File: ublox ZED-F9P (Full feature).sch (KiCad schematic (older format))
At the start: 99 parts, among them J1 USB_C_2-LAYER_PADS, J2 CONN_06NO_SILK_FEMALE_PTH, J3 Molex_PicoBlade, J4 PinHeader, J5 USB_C_2-LAYER_PADS, J6 CONN_06NO_SILK_FEMALE_PTH, J7 JST_GH, U1 LD1117S33TR, U3 ZED-F9P, U4 ZED-F9H

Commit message: part no updated
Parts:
- removed J3: Molex_PicoBlade, Connector_Molex:Molex_PicoBlade_53261-0671_1x06-1MP_P1.25mm_Horizontal, symbol Connector:Conn_01x06_Male
- removed JP1, JP2, JP3, JP4: Jumper_NO_Small, Jumper:SolderJumper-2_P1.3mm_Open_RoundedPad1.0x1.5mm, symbol Device:Jumper_NO_Small
- removed LED1: RED, Qwiic GPS-RTK-SMA - ublox ZED-F9P:LED-0603, symbol ublox-ZED-F9P-(Full-feature)-rescue:LED-RED0603-Qwiic_GPS-RTK-SMA_-_ublox_ZED-F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
- removed PPS1, PWR2: JUMPER-SMT_2_NC_TRACE_SILK, Qwiic GPS-RTK-SMA - ublox ZED-F9P:SMT-JUMPER_2_NC_TRACE_SILK, symbol ublox-ZED-F9P-(Full-feature)-rescue:JUMPER-SMT_2_NC_TRACE_SILK-Qwiic_GPS-RTK-SM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
- removed R34: 1k, Qwiic GPS-RTK-SMA - ublox ZED-F9P:0603, symbol ublox-ZED-F9P-(Full-feature)-rescue:1KOHM-0603-1_10W-1%-Qwiic_GPS-RTK-SMA_-_ubl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
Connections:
- net at R21.1: now also E2.SIG (SIGNAL), U3.53 (TIMEPULSE)
- net RX(#4) renamed RX_P
- net RX(#5) renamed RX_H
- net TX(#4) renamed TX_P
- net TX(#5) renamed TX_H
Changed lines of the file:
@@
 Wire Wire Line
 	10775 2925 10475 2925
-Wire Wire Line
-	13425 6925 13425 6825
-Text Label 13425 6925 0    10   ~ 0
-3.3V
-Wire Wire Line
-	13425 8325 13425 8225
-Text Label 13425 8325 0    10   ~ 0
-GND
-Wire Wire Line
-	13425 7925 13425 7825
-Wire Wire Line
-	13425 7325 13425 7425
-$Comp
-L ublox-ZED-F9P-(Full-feature)-rescue:1KOHM-0603-1_10W-1%-Qwiic_GPS-RTK-SMA_-_ublox_ZED-F9P-eagle-import R34
-U 1 1 5F77C25B
-P 13425 7625
-F 0 "R34" H 13280 7540 70  0000 C BNN
-F 1 "1k" H 13605 7605 70  0000 C TNN
-F 2 "Qwiic GPS-RTK-SMA - ublox ZED-F9P:0603" H 13425 7625 50  0001 C CNN
-F 3 "" H 13425 7625 50  0001 C CNN
-F 4 "ERJ-3EKF1001V" H 13425 7625 50  0001 C CNN "partno"
-	1    13425 7625
-	0    -1   -1   0
-$EndComp
-$Comp
-L ublox-ZED-F9P-(Full-feature)-rescue:LED-RED0603-Qwiic_GPS-RTK-SMA_-_ublox_ZED-F9P-eagle-import LED1
-U 1 1 5F77C265
-P 13425 8025
-F 0 "LED1" V 13410 7645 70  0000 L BNN
-F 1 "RED" V 13445 7705 70  0000 L TNN
-F 2 "Qwiic GPS-RTK-SMA - ublox ZED-F9P:LED-0603" H 13425 8025 50  0001 C CNN
-F 3 "" H 13425 8025 50  0001 C CNN
-F 4 "HSMH-C191" H 13425 8025 50  0001 C CNN "partno"
-	1    13425 8025
-	1    0    0    -1
-$EndComp
-$Comp
-L ublox-ZED-F9P-(Full-feature)-rescue:GND-Qwiic_GPS-RTK-SMA_-_ublox_ZED-F9P-eagle-import #GND0110
-U 1 1 5F77C26F
-P 13425 8425
-F 0 "#GND0110" H 13425 8425 50  0001 C CNN
-F 1 "GND" H 13325 8325 59  0000 L BNN
-F 2 "" H 13425 8425 50  0001 C CNN
-F 3 "" H 13425 8425 50  0001 C CNN
-	1    13425 8425
-	1    0    0    -1
-$EndComp
-$Comp
-L ublox-ZED-F9P-(Full-feature)-rescue:3.3V-Qwiic_GPS-RTK-SMA_-_ublox_ZED-F9P-eagle-import #P+0101
-U 1 1 5F77C279
-P 13425 6825
-F 0 "#P+0101" H 13425 6825 50  0001 C CNN
-F 1 "3.3V" H 13425 6935 59  0000 C BNN
-F 2 "" H 13425 6825 50  0001 C CNN
-F 3 "" H 13425 6825 50  0001 C CNN
-	1    13425 6825
-	1    0    0    -1
-$EndComp
-$Comp
-L ublox-ZED-F9P-(Full-feature)-rescue:JUMPER-SMT_2_NC_TRACE_SILK-Qwiic_GPS-RTK-SMA_-_ublox_ZED-F9P-eagle-import PWR2
-U 1 1 5F77C283
-P 13425 7125
-F 0 "PWR2" H 13345 7195 70  0000 L BNN
-F 1 "JUMPER-SMT_2_NC_TRACE_SILK" H 13325 7025 70  0000 L TNN
-F 2 "Qwiic GPS-RTK-SMA - ublox ZED-F9P:SMT-JUMPER_2_NC_TRACE_SILK" H 13425 7125 50  0001 C CNN
-F 3 "" H 13425 7125 50  0001 C CNN
-F 4 "-" H 13425 7125 50  0001 C CNN "partno"
-	1    13425 7125
-	0    -1   -1   0
-$EndComp
 Text Notes 13825 5100 0    85   ~ 17
 Stat LEDs (F9H)
@@
 Wire Wire Line
 	12625 2725 12775 2725
-$Comp
-L Connector:Conn_01x06_Male J3
-U 1 1 5F708564
-P 16425 2900
-F 0 "J3" H 16531 3278 50  0000 C CNN
-F 1 "Molex_PicoBlade" H 16250 3200 50  0000 C CNN
-F 2 "Connector_Molex:Molex_PicoBlade_53261-0671_1x06-1MP_P1.25mm_Horizontal" H 16425 2900 50  0001 C CNN
-F 3 "https://www.digikey.com/product-detail/en/molex/0532610671/WM7624CT-ND/699111" H 16425 2900 50  0001 C CNN
-F 4 "0532610671" H 16425 2900 50  0001 C CNN "partno"
-F 5 "Connector Header Surface Mount, Right Angle 6 position 0.049\" (1.25mm)" H 16425 2900 50  0001 C CNN "Detailed Description"
-F 6 "Approved" H 16425 2900 50  0001 C CNN "Approval"
-	1    16425 2900
-	1    0    0    -1
-$EndComp
 $Comp
 L Connector:Conn_01x06_Male J4
@@
 	1    0    0    -1
 $EndComp
-Wire Wire Line
-	16625 2700 16875 2700
 Connection ~ 16875 2700
 Wire Wire Line
@@
 Wire Wire Line
 	16875 2700 16875 3525
-Text Label 17225 2700 0    50   ~ 0
-Vcc
-Wire Wire Line
-	16625 3200 17250 3200
 Wire Wire Line
 	17250 3200 17500 3200
-Connection ~ 17250 3200
 Wire Wire Line
 	17250 4025 17250 3200
@@
 Wire Wire Line
 	17175 3100 17175 3925
-Text Label 17225 2800 0    50   ~ 0
-RX(#4)
-Text Label 17225 2900 0    50   ~ 0
-TX(#4)
-Text Label 17225 3000 0    50   ~ 0
-RX(#5)
-Text Label 17225 3100 0    50   ~ 0
-TX(#5)
-Text Label 17225 3200 0    50   ~ 0
-GND
 Wire Notes Line
 	15850 1950 15850 4250
@@
 	16875 2525 16875 2700
 $Comp
-L Device:Jumper_NO_Small JP1
-U 1 1 5F7085B9
-P 16725 2800
-F 0 "JP1" H 16725 2850 50  0000 C CNN
-F 1 "Jumper_NO_Small" H 16725 2894 50  0001 C CNN
-F 2 "Jumper:SolderJumper-2_P1.3mm_Open_RoundedPad1.0x1.5mm" H 16725 2800 50  0001 C CNN
-F 3 "~" H 16725 2800 50  0001 C CNN
-F 4 "Approved" H 16725 2800 50  0001 C CNN "Approval"
-F 5 "-" H 16725 2800 50  0001 C CNN "partno"
-	1    16725 2800
-	1    0    0    -1
-$EndComp
-Wire Wire Line
-	16825 2800 16950 2800
-$Comp
-L Device:Jumper_NO_Small JP2
-U 1 1 5F7085C1
-P 16725 2900
-F 0 "JP2" H 16725 2950 50  0000 C CNN
-F 1 "Jumper_NO_Small" H 16725 2994 50  0001 C CNN
-F 2 "Jumper:SolderJumper-2_P1.3mm_Open_RoundedPad1.0x1.5mm" H 16725 2900 50  0001 C CNN
-F 3 "~" H 16725 2900 50  0001 C CNN
-F 4 "Approved" H 16725 2900 50  0001 C CNN "Approval"
-F 5 "-" H 16725 2900 50  0001 C CNN "partno"
-	1    16725 2900
-	1    0    0    -1
-$EndComp
-Wire Wire Line
-	16825 2900 17025 2900
-$Comp
-L Device:Jumper_NO_Small JP3
-U 1 1 5F7085C9
-P 16725 3000
-F 0 "JP3" H 16725 3050 50  0000 C CNN
-F 1 "Jumper_NO_Small" H 16725 3094 50  0001 C CNN
-F 2 "Jumper:SolderJumper-2_P1.3mm_Open_RoundedPad1.0x1.5mm" H 16725 3000 50  0001 C CNN
-F 3 "~" H 16725 3000 50  0001 C CNN
-F 4 "Approved" H 16725 3000 50  0001 C CNN "Approval"
-F 5 "-" H 16725 3000 50  0001 C CNN "partno"
-	1    16725 3000
-	1    0    0    -1
-$EndComp
-Wire Wire Line
-	16825 3000 17100 3000
-$Comp
-L Device:Jumper_NO_Small JP4
-U 1 1 5F7085D1
-P 16725 3100
-F 0 "JP4" H 16725 3150 50  0000 C CNN
-F 1 "Jumper_NO_Small" H 16725 3194 50  0001 C CNN
-F 2 "Jumper:SolderJumper-2_P1.3mm_Open_RoundedPad1.0x1.5mm" H 16725 3100 50  0001 C CNN
-F 3 "~" H 16725 3100 50  0001 C CNN
-F 4 "Approved" H 16725 3100 50  0001 C CNN "Approval"
-F 5 "-" H 16725 3100 50  0001 C CNN "partno"
-	1    16725 3100
-	1    0    0    -1
-$EndComp
-Wire Wire Line
-	16825 3100 17175 3100
-$Comp
 L Device:Jumper_NO_Small JP5
 U 1 1 5F7085D9
@@
 $EndComp
 Wire Wire Line
-	6100 3600 6000 3600
-Wire Wire Line
-	5500 3600 5600 3600
-$Comp
-L ublox-ZED-F9P-(Full-feature)-rescue:JUMPER-SMT_2_NC_TRACE_SILK-Qwiic_GPS-RTK-SMA_-_ublox_ZED-F9P-eagle-import PPS1
-U 1 1 E4382B22
-P 5800 3600
-F 0 "PPS1" H 5900 3740 70  0000 R TNN
-F 1 "JUMPER-SMT_2_NC_TRACE_SILK" H 5700 3500 70  0000 L TNN
-F 2 "Qwiic GPS-RTK-SMA - ublox ZED-F9P:SMT-JUMPER_2_NC_TRACE_SILK" H 5800 3600 50  0001 C CNN
-F 3 "" H 5800 3600 50  0001 C CNN
-F 4 "-" H 5800 3600 50  0001 C CNN "partno"
-	1    5800 3600
-	-1   0    0    1
-$EndComp
-Wire Wire Line
 	10000 6725 10375 6725
 Wire Wire Line
@@
 	1    0    0    1
 $EndComp
+Text Label 17225 2800 0    50   ~ 0
+RX_P
+Text Label 17225 2900 0    50   ~ 0
+TX_P
+Text Label 17225 3000 0    50   ~ 0
+RX_H
+Text Label 17225 3100 0    50   ~ 0
+TX_H
+Text Label 17225 2700 0    50   ~ 0
+Vcc
+Wire Wire Line
+	5500 3600 6100 3600
 $EndSCHEMATC

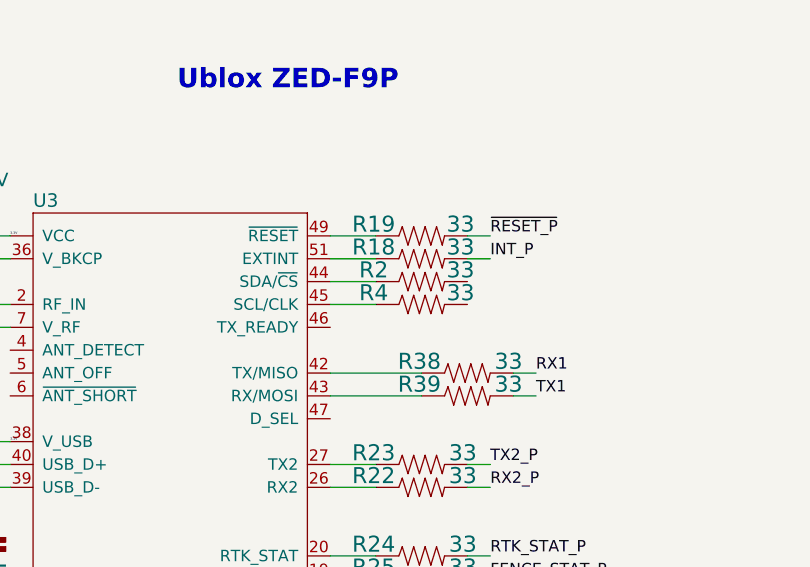
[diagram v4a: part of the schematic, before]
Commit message: removed unescessary resistors
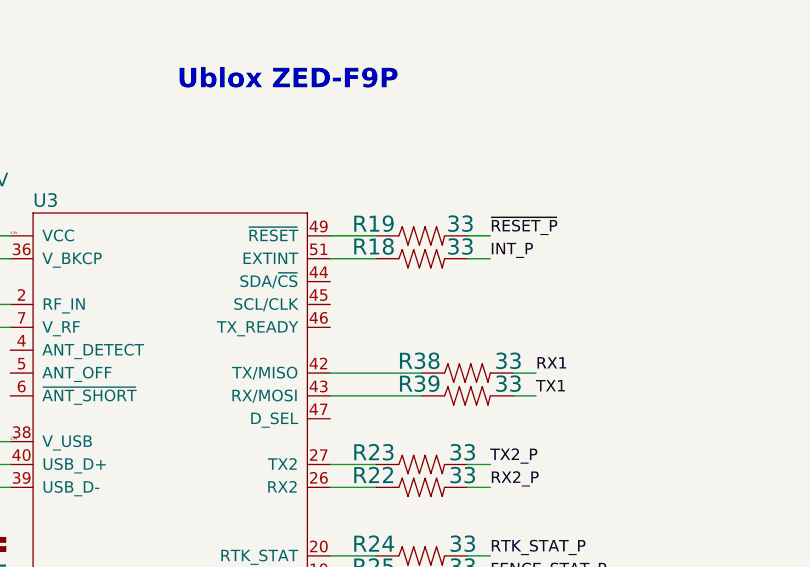
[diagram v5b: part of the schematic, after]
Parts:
- removed R2, R4: 33, Qwiic GPS-RTK-SMA - ublox ZED-F9P:0603, symbol ublox-ZED-F9P-(Full-feature)-rescue:33OHM-0603-1_10W-1%-Qwiic_GPS-RTK-SMA_-_ubl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
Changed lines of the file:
@@
 	1800 6000 1800 6100
-Wire Wire Line
-	5500 2200 5300 2200
-Wire Wire Line
-	5500 2300 5300 2300
 Wire Wire Line
 	3125 9575 3025 9575
@@
 	1    0    0    -1
 $EndComp
-$Comp
-L ublox-ZED-F9P-(Full-feature)-rescue:33OHM-0603-1_10W-1%-Qwiic_GPS-RTK-SMA_-_ublox_ZED-F9P-eagle-import R4
-U 1 1 83B45A75
-P 5700 2300
-F 0 "R4" H 5490 2310 70  0000 C BNN
-F 1 "33" H 5870 2310 70  0000 C BNN
-F 2 "Qwiic GPS-RTK-SMA - ublox ZED-F9P:0603" H 5700 2300 50  0001 C CNN
-F 3 "" H 5700 2300 50  0001 C CNN
-F 4 "ERJ-3EKF27R0V" H 5700 2300 50  0001 C CNN "partno"
-	1    5700 2300
-	1    0    0    -1
-$EndComp
-$Comp
-L ublox-ZED-F9P-(Full-feature)-rescue:33OHM-0603-1_10W-1%-Qwiic_GPS-RTK-SMA_-_ublox_ZED-F9P-eagle-import R2
-U 1 1 250F4BD6
-P 5700 2200
-F 0 "R2" H 5490 2210 70  0000 C BNN
-F 1 "33" H 5870 2210 70  0000 C BNN
-F 2 "Qwiic GPS-RTK-SMA - ublox ZED-F9P:0603" H 5700 2200 50  0001 C CNN
-F 3 "" H 5700 2200 50  0001 C CNN
-F 4 "ERJ-3EKF27R0V" H 5700 2200 50  0001 C CNN "partno"
-	1    5700 2200
-	1    0    0    -1
-$EndComp

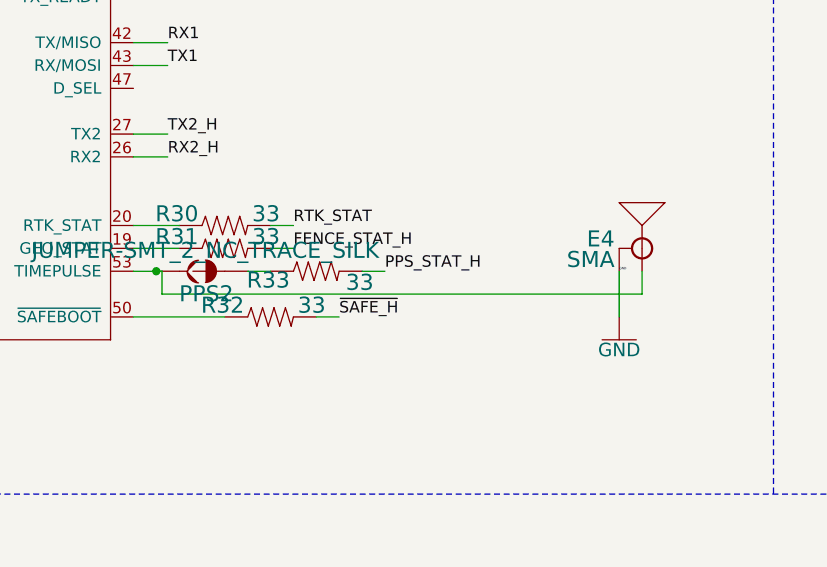
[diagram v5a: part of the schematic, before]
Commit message: removed SMA time paulse from F9H
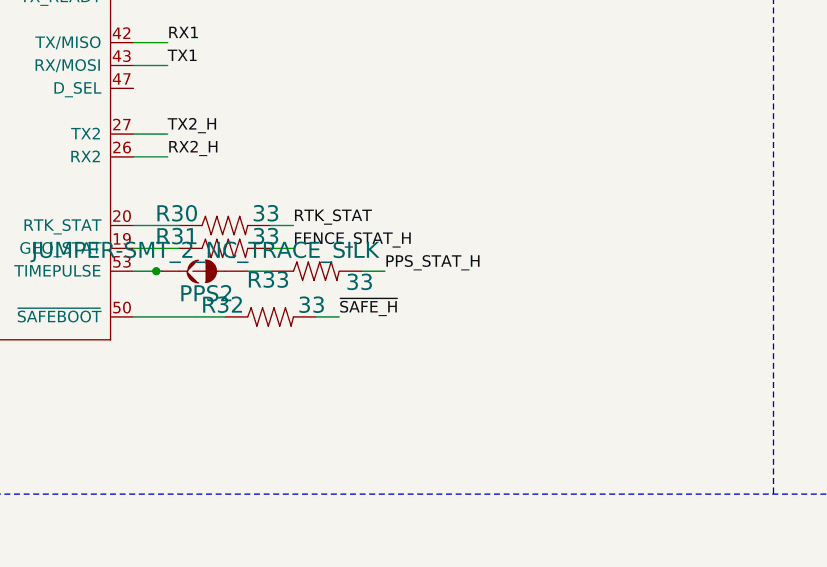
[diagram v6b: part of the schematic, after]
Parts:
- removed E4: SMA, Qwiic GPS-RTK-SMA - ublox ZED-F9P:SMA-EDGE, symbol ublox-ZED-F9P-(Full-feature)-rescue:ANTENNA-GROUNDEDEDGE_SMA-Qwiic_GPS-RTK-SMA_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
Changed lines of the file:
@@
 PPS_STAT_H
 Wire Wire Line
-	14750 3625 14750 3825
-Text Label 14750 3625 0    10   ~ 0
-GND
-Wire Wire Line
-	12750 3725 14850 3725
-Wire Wire Line
-	14850 3725 14850 3625
-$Comp
-L ublox-ZED-F9P-(Full-feature)-rescue:ANTENNA-GROUNDEDEDGE_SMA-Qwiic_GPS-RTK-SMA_-_ublox_ZED-F9P-eagle-import E4
-U 1 1 5F653EF8
-P 14850 3525
-F 0 "E4" H 14970 3525 70  0000 L BNN
-F 1 "SMA" H 14970 3435 70  0000 L BNN
-F 2 "Qwiic GPS-RTK-SMA - ublox ZED-F9P:SMA-EDGE" H 14850 3525 50  0001 C CNN
-F 3 "https://www.digikey.com/product-detail/en/rf-solutions/CON-SMA-EDGE-S/CON-SMA-EDGE-S-ND/5845767" H 14850 3525 50  0001 C CNN
-F 4 "CON-SMA-EDGE-S" H 14850 3525 50  0001 C CNN "partno"
-	1    14850 3525
-	-1   0    0    -1
-$EndComp
-$Comp
-L ublox-ZED-F9P-(Full-feature)-rescue:GND-Qwiic_GPS-RTK-SMA_-_ublox_ZED-F9P-eagle-import #GND0105
-U 1 1 5F653F02
-P 14750 3925
-F 0 "#GND0105" H 14750 3925 50  0001 C CNN
-F 1 "GND" H 14750 3915 59  0000 C TNN
-F 2 "" H 14750 3925 50  0001 C CNN
-F 3 "" H 14750 3925 50  0001 C CNN
-	1    14750 3925
-	1    0    0    -1
-$EndComp
-Wire Wire Line
 	12725 3625 12750 3625
-Wire Wire Line
-	12750 3625 12750 3725
 Connection ~ 12725 3625
 Wire Wire Line

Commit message: removed SMA time paulse from F9H
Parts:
- removed B1: 6.8MM_COIN_CELL, Qwiic GPS-RTK-SMA - ublox ZED-F9P:ML414H_IV01E, symbol ublox-ZED-F9P-(Full-feature)-rescue:ML414H_IV01E_BATTERY-Qwiic_GPS-RTK-SMA_-_ub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
- added BT1: Battery_Cell, Qwiic GPS-RTK-SMA - ublox ZED-F9P:ML414H_IV01E, symbol Device:Battery_Cell
- J4: value PinHeader -> Molex_PicoBlade; footprint HG_Footprints:5-103635-5 -> Connector_Molex:Molex_PicoBlade_53261-0671_1x06-1MP_P1.25mm_Horizontal; Detailed Description Connector Header Through Hole, Right Angle 6 position 0.100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 -> Connector Header Surface Mount, Right Angle 6 position 0.04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; Series SL -> (none); partno 0705530110 -> 0532610671
- U4: footprint (none) -> Qwiic GPS-RTK-SMA - ublox ZED-F9P:ZED-F9P
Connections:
- net 3.3V is gone; now on net +3V3: C2.1, C4.2, C7.2, D2.A, PWR1.2, R15.2, U1.2 (VO), U3.33 (VCC), U3.34 (VCC), U3.38 (V_USB)
- net INT is gone; now on net INT_H: J2.6
- net RTK_STAT is gone; now on net RTK_STAT_H: R30.2
- net RX_H is gone; now on net RX2_H: J4.4 (Pin_4), JP7.2
- net RX_P is gone; now on net RX2_P: J4.2 (Pin_2), JP5.2
- net TX_H is gone; now on net TX2_H: J4.5 (Pin_5), JP8.2
- net TX_P is gone; now on net TX2_P: J4.3 (Pin_3), JP6.2
- net +5V: now also C5.2, D7.1 (K), D8.1 (K), U1.3 (VI)
- net BACKUP: now also BT1.1 (+)
- net GND: now also BT1.2 (-)
- net +3V3: now reaches U4.33 (VCC), U4.34 (VCC)
- net +3V3: now also C10.1, C11.2, R27.2, U4.38 (V_USB)
- net Vcc: no longer names the net of D12.2 (A), J4.1 (Pin_1), J7.1 (Pin_1)
- no-connect marks 0 -> 14
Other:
- note removed: "same backup battery?"

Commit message: changed usb c
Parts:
- removed J1: USB_C_2-LAYER_PADS, Qwiic GPS-RTK-SMA - ublox ZED-F9P:USB-C-16P-2LAYER-PADS, symbol ublox-ZED-F9P-(Full-feature)-rescue:USB_C_2-LAYER_PADS-Qwiic_GPS-RTK-SMA_-_ublo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
- removed JP5, JP6, JP7, JP8: Jumper_NO_Small, Jumper:SolderJumper-2_P1.3mm_Open_RoundedPad1.0x1.5mm, symbol Device:Jumper_NO_Small
- removed PWR1: JUMPER-SMT_2_NC_TRACE_SILK, Qwiic GPS-RTK-SMA - ublox ZED-F9P:SMT-JUMPER_2_NC_TRACE_SILK, symbol ublox-ZED-F9P-(Full-feature)-rescue:JUMPER-SMT_2_NC_TRACE_SILK-Qwiic_GPS-RTK-SM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
- added H1, H2, H3, H4: MountingHole, MountingHole:MountingHole_3.2mm_M3, symbol Mechanical:MountingHole
- added J1, J3: USB_C_Receptacle, symbol Connector:USB_C_Receptacle
- BT1: symbol Device:Battery_Cell -> ublox-ZED-F9P-(Full-feature)-rescue:ML414H_IV01E_BATTERY-Qwiic_GPS-RTK-SMA_-_ublox_ZED-F9P-eagle-import
- FB1: Detailed Description 180 Ohms @ 100MHz 1 Ferrite Bead 0603 (1608 Metric) 2A 50mOhm -> 180 Ohms @ 100MHz 1 Ferrite Bead 0603 (1608 Metric) 2A 50mOhm
- J5: footprint Qwiic GPS-RTK-SMA - ublox ZED-F9P:USB-C-16P-2LAYER-PADS -> Connector_USB:USB_C_Receptacle_GCT_USB4085; partno USB-C31-S-RA-EH2.0B-BK-T/R -> USB4085-GF-A
- renumbered LED2 to LED1, D1 to LED2, D3 to LED3, D4 to LED4, D9 to LED5, D10 to LED6, D11 to LED7
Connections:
- net +3V3: now also R1.2
- net BACKUP: now also BT1.+; no longer BT1.1 (+)
- net GND: no longer BT1.2 (-), D5.2, J4.6 (Pin_6), J5.GND, J5.GND2 (GND), J5.SHLD1 (SHLD), J5.SHLD2 (SHLD), J5.SHLD3 (SHLD), J5.SHLD4 (SHLD), J7.6 (Pin_6)
- net RX2_H: now also J7.4 (Pin_4)
- net RX2_P: now also J7.2 (Pin_2)
- net TX2_H: now also J7.5 (Pin_5)
- net TX2_P: now also J7.3 (Pin_3)
- net VBUS: now reaches C6.1, D6.5, D7.2 (A)
- net VBUS: now also C9.1, D5.5, D8.2 (A), J1.A4 (VBUS), J1.A9 (VBUS), J1.B4 (VBUS), J1.B9 (VBUS), J3.A4 (VBUS), J3.A9 (VBUS), J3.B4 (VBUS), J3.B9 (VBUS); no longer J5.VBUS1 (VBUS), J5.VBUS2 (VBUS)
- net at J5.A5 (CC1): no longer R17.2
- net at J5.A6 (D+), J5.B6 (D+): no longer D6.3
- net at J5.A7 (D-), J5.B7 (D-): no longer D6.1
- net at J5.B5 (CC2): no longer R16.2
- net at R3.2: now also J3.B5 (CC2)
- net at R6.2: now also J3.A5 (CC1)
- net at D5.3: now also J3.A6 (D+), J3.B6 (D+)
- net at D5.1: now also J3.A7 (D-), J3.B7 (D-)
- new net: J5.GND, J5.GND2 (GND)
- new net: J5.SHLD1 (SHLD), J5.SHLD2 (SHLD), J5.SHLD3 (SHLD), J5.SHLD4 (SHLD)
- new net: J5.VBUS1 (VBUS), J5.VBUS2 (VBUS)
- new net: J4.6 (Pin_6), J7.6 (Pin_6)
- new net: J1.A1 (GND), J1.A12 (GND), J1.B1 (GND), J1.B12 (GND), J1.S1 (SHIELD)
- new net: J1.A5 (CC1), R17.2
- new net: D6.3, J1.A6 (D+), J1.B6 (D+)
- new net: D6.1, J1.A7 (D-), J1.B7 (D-)
- new net: J1.B5 (CC2), R16.2
- new net: J3.A1 (GND), J3.A12 (GND), J3.B1 (GND), J3.B12 (GND), J3.S1 (SHIELD)
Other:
- moved on the sheet: C4, C5, C6, C9, D5, D6, D7, D8, J2, J5, R16, R17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
